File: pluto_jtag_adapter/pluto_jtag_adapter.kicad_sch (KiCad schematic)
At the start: 61 parts, among them J1 JTAG_UART_PLUTO, J2 Conn_01x08, J3 Conn_01x04, J4 USB_B_Micro, U1 FT2232HL, U2 AP2112K-3.3, U3 AP2112K-1.8, U4 93LC46B, U6 TXB0104D, U7 TLV7031DBV, U8 WE-TVS-82400102, U9 TXB0102DCU, Y1 7M-12.000MAAJ-T

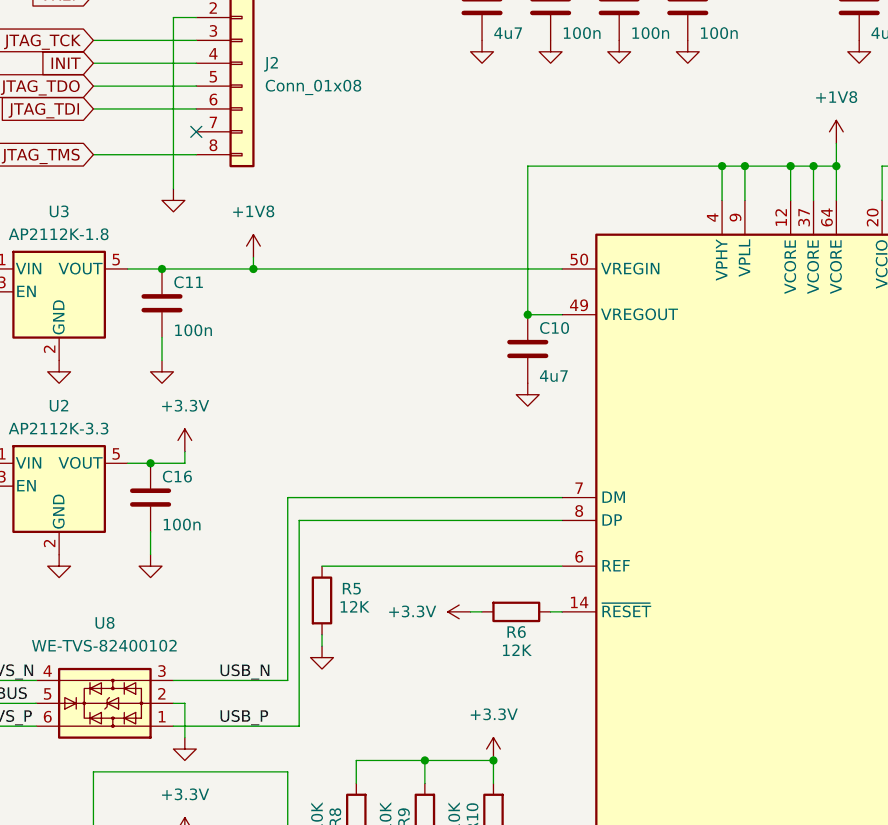
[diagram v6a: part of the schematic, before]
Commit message: Disconnect VREGIN and VREGOUT
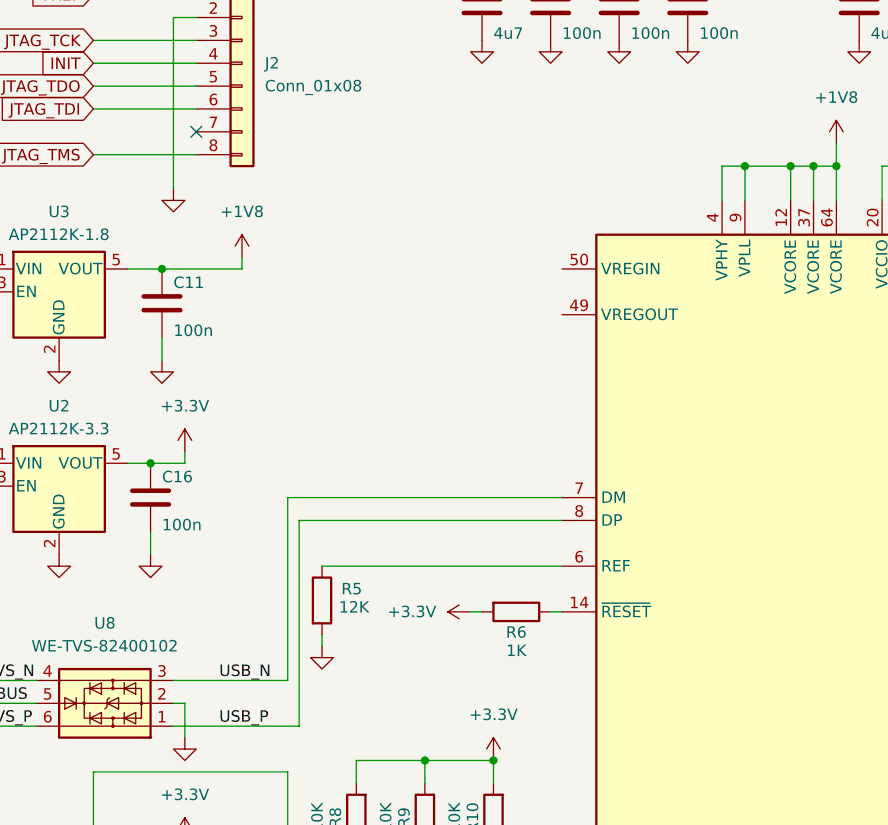
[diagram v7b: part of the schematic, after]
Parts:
- removed C10: 4u7, Capacitor_SMD:C_0603_1608Metric_Pad1.08x0.95mm_HandSolder, symbol Device:C
- R6: value 12K -> 1K
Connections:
- net +1V8: no longer U1.49 (VREGOUT), U1.50 (VREGIN)
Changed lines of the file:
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@@
 	)
 	(junction
-		(at 101.6 86.36)
-		(diameter 0)
-		(color 0 0 0 0)
-	)
-	(junction
 		(at 218.44 121.92)
 		(diameter 0)
@@
 	)
 	(junction
-		(at 71.12 81.28)
-		(diameter 0)
-		(color 0 0 0 0)
-	)
-	(junction
-		(at 123.19 69.85)
-		(diameter 0)
-		(color 0 0 0 0)
-	)
-	(junction
 		(at 60.96 81.28)
 		(diameter 0)
@@
 	(wire
 		(pts
-			(xy 101.6 69.85) (xy 123.19 69.85)
-		)
-		(stroke
-			(width 0)
-			(type default)
-		)
-	)
-	(wire
-		(pts
 			(xy 99.06 152.4) (xy 105.41 152.4)
 		)
@@
 	(wire
 		(pts
-			(xy 101.6 86.36) (xy 105.41 86.36)
-		)
-		(stroke
-			(width 0)
-			(type default)
-		)
-	)
-	(wire
-		(pts
 			(xy 73.66 154.94) (xy 82.55 154.94)
 		)
@@
 	(wire
 		(pts
-			(xy 101.6 69.85) (xy 101.6 86.36)
-		)
-		(stroke
-			(width 0)
-			(type default)
-		)
-	)
-	(wire
-		(pts
 			(xy 82.55 138.43) (xy 82.55 135.89)
 		)
@@
 	(wire
 		(pts
-			(xy 71.12 81.28) (xy 71.12 80.01)
+			(xy 69.85 81.28) (xy 69.85 80.01)
 		)
 		(stroke
@@
 	(wire
 		(pts
-			(xy 60.96 81.28) (xy 71.12 81.28)
+			(xy 60.96 81.28) (xy 69.85 81.28)
 		)
 		(stroke
@@
 	(wire
 		(pts
-			(xy 71.12 81.28) (xy 105.41 81.28)
-		)
-		(stroke
-			(width 0)
-			(type default)
-		)
-	)
-	(wire
-		(pts
 			(xy 166.37 127) (xy 168.91 127)
 		)
@@
 	)
 	(symbol
-		(lib_id "Device:C")
-		(at 101.6 90.17 0)
-		(unit 1)
-		(exclude_from_sim no)
-		(in_bom yes)
-		(on_board yes)
-		(dnp no)
-		(property "Reference" "C10"
-			(at 102.87 87.884 0)
-			(effects
-				(font
-					(size 1.27 1.27)
-				)
-				(justify left)
-			)
-		)
-		(property "Value" "4u7"
-			(at 102.87 93.218 0)
-			(effects
-				(font
-					(size 1.27 1.27)
-				)
-				(justify left)
-			)
-		)
-		(property "Footprint" "Capacitor_SMD:C_0603_1608Metric_Pad1.08x0.95mm_HandSolder"
-			(at 102.5652 93.98 0)
-			(effects
-				(font
-					(size 1.27 1.27)
-				)
-				(hide yes)
-			)
-		)
-		(property "Datasheet" "~"
-			(at 101.6 90.17 0)
-			(effects
-				(font
-					(size 1.27 1.27)
-				)
-				(hide yes)
-			)
-		)
-		(property "Description" "Unpolarized capacitor"
-			(at 101.6 90.17 0)
-			(effects
-				(font
-					(size 1.27 1.27)
-				)
-				(hide yes)
-			)
-		)
-		(pin "1"
-		)
-		(pin "2"
-		)
-		(instances
-			(project "pluto_jtag_adapter"
-				(path "/3be8ddee-85ba-421c-a851-ede1499a4287"
-					(reference "C10")
-					(unit 1)
-				)
-			)
-		)
-	)
-	(symbol
 		(lib_id "power:+1V8")
 		(at 135.89 67.31 0)
@@
 	(symbol
 		(lib_id "power:+1V8")
-		(at 71.12 80.01 0)
+		(at 69.85 80.01 0)
 		(unit 1)
 		(exclude_from_sim no)
@@
 		(fields_autoplaced yes)
 		(property "Reference" "#PWR012"
-			(at 71.12 83.82 0)
+			(at 69.85 83.82 0)
 			(effects
 				(font
@@
 		)
 		(property "Value" "+1V8"
-			(at 71.12 74.93 0)
+			(at 69.85 74.93 0)
 			(effects
 				(font
@@
 		)
 		(property "Footprint" ""
-			(at 71.12 80.01 0)
+			(at 69.85 80.01 0)
 			(effects
 				(font
@@
 		)
 		(property "Datasheet" ""
-			(at 71.12 80.01 0)
+			(at 69.85 80.01 0)
 			(effects
 				(font
@@
 		)
 		(property "Description" "Power symbol creates a global label with name \"+1V8\""
-			(at 71.12 80.01 0)
+			(at 69.85 80.01 0)
 			(effects
 				(font
@@
 			)
 		)
-		(property "Value" "12K"
+		(property "Value" "1K"
 			(at 100.33 123.698 90)
 			(effects
@@
 					(unit 1)
 				)
-			)
-		)
-	)
-	(symbol
-		(lib_id "power:GND")
-		(at 101.6 93.98 0)
-		(unit 1)
-		(exclude_from_sim no)
-		(in_bom yes)
-		(on_board yes)
-		(dnp no)
-		(fields_autoplaced yes)
-		(property "Reference" "#PWR031"
-			(at 101.6 100.33 0)
-			(effects
-				(font
-					(size 1.27 1.27)
-				)
-				(hide yes)
-			)
-		)
-		(property "Value" "GND"
-			(at 101.6 99.06 0)
-			(effects
-				(font
-					(size 1.27 1.27)
-				)
-				(hide yes)
-			)
-		)
-		(property "Footprint" ""
-			(at 101.6 93.98 0)
-			(effects
-				(font
-					(size 1.27 1.27)
-				)
-				(hide yes)
-			)
-		)
-		(property "Datasheet" ""
-			(at 101.6 93.98 0)
-			(effects
-				(font
-					(size 1.27 1.27)
-				)
-				(hide yes)
-			)
-		)
-		(property "Description" "Power symbol creates a global label with name \"GND\" , ground"
-			(at 101.6 93.98 0)
-			(effects
-				(font
-					(size 1.27 1.27)
-				)
-				(hide yes)
-			)
-		)
-		(pin "1"
-		)
-		(instances
-			(project "pluto_jtag_adapter"
-				(path "/3be8ddee-85ba-421c-a851-ede1499a4287"
-					(reference "#PWR031")
-					(unit 1)
-				)

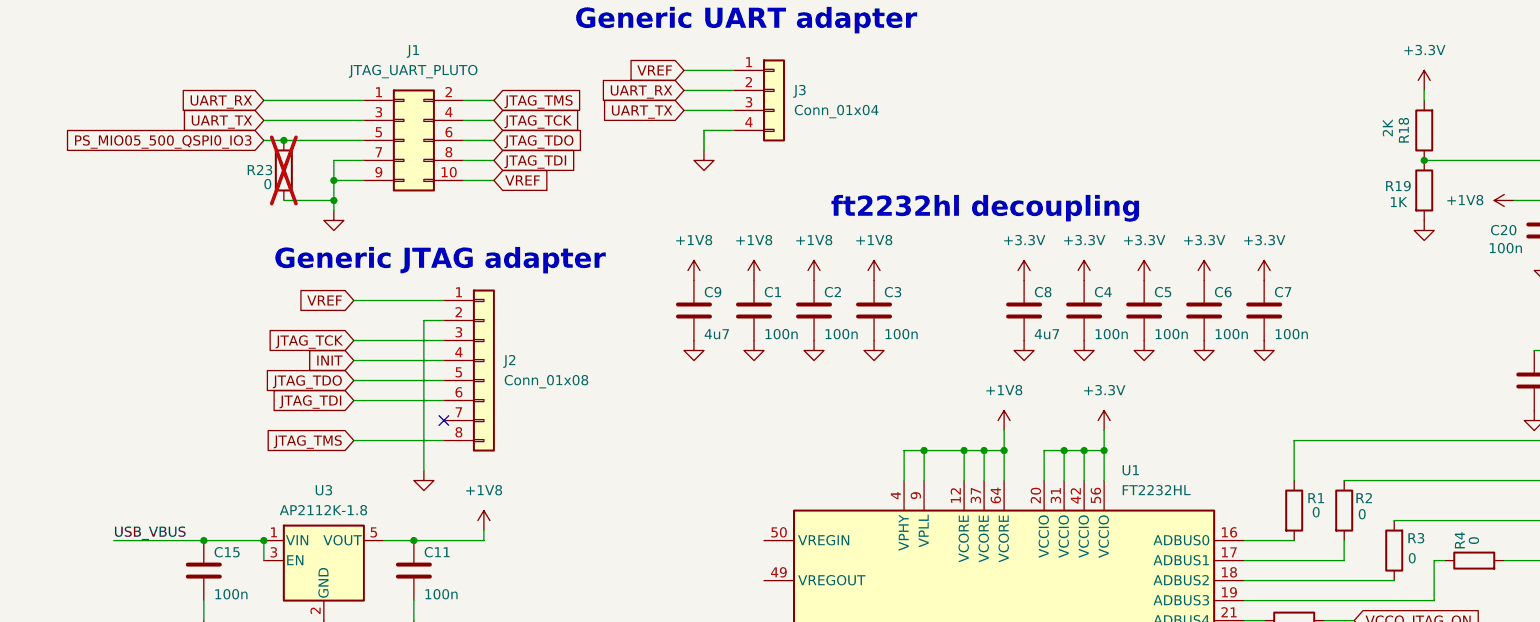
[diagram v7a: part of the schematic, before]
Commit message: Add correct supplies for VPHY and VPLL
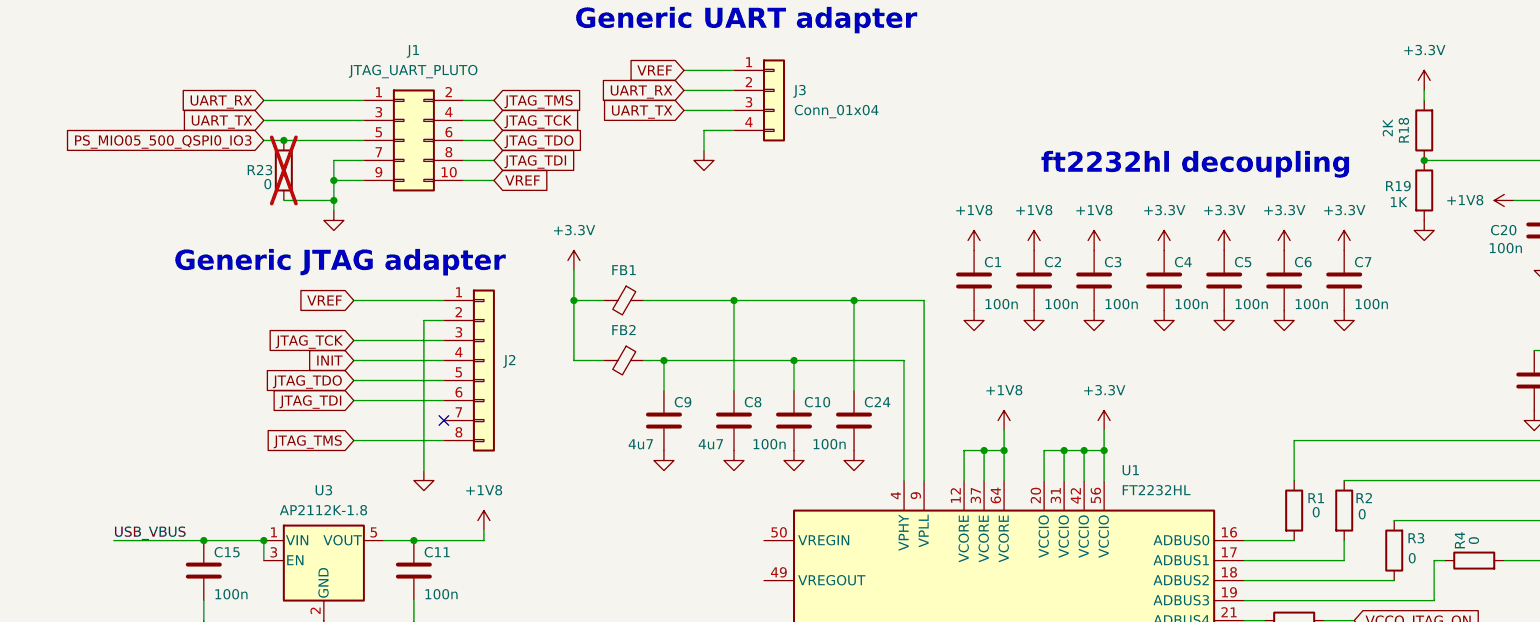
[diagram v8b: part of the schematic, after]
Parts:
- added C10, C24: 100n, Capacitor_SMD:C_0603_1608Metric_Pad1.08x0.95mm_HandSolder, symbol Device:C
- added FB1, FB2: BLM18BA121SH1D, Inductor_SMD:L_0603_1608Metric, symbol Device:FerriteBead_Small
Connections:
- net +1V8: no longer C9.1, U1.4 (VPHY), U1.9 (VPLL)
- net +3.3V: now also FB1.2, FB2.2; no longer C8.1
- net GND: now also C10.2, C24.2
- new net: C10.1, C9.1, FB2.1, U1.4 (VPHY)
- new net: C24.1, C8.1, FB1.1, U1.9 (VPLL)
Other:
- moved on the sheet: C1, C2, C3, C4, C5, C6, C7, C8, C9
